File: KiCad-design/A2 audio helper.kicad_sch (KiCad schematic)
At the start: 37 parts, among them J1 PIN HEADER 1x2, J10 PIN HEADER 1x2, J11 PIN HEADER 1x3, J12 PIN HEADER 1x3, J13 PIN HEADER 2x4, J14 PIN HEADER 1x3, J15 PIN HEADER 2x6, J2 PIN HEADER 1x2, J3 PIN HEADER 1x2, J4 SJ1-3515N, J5 PIN HEADER 1x3, J6 PIN HEADER 1x3, J7 SJ1-3515N, J8 PIN HEADER 1x5, J9 PIN HEADER 1x2, K1 SR11-5V-200-2C, SW2 SW_DPDT_x2, U1 pam8403

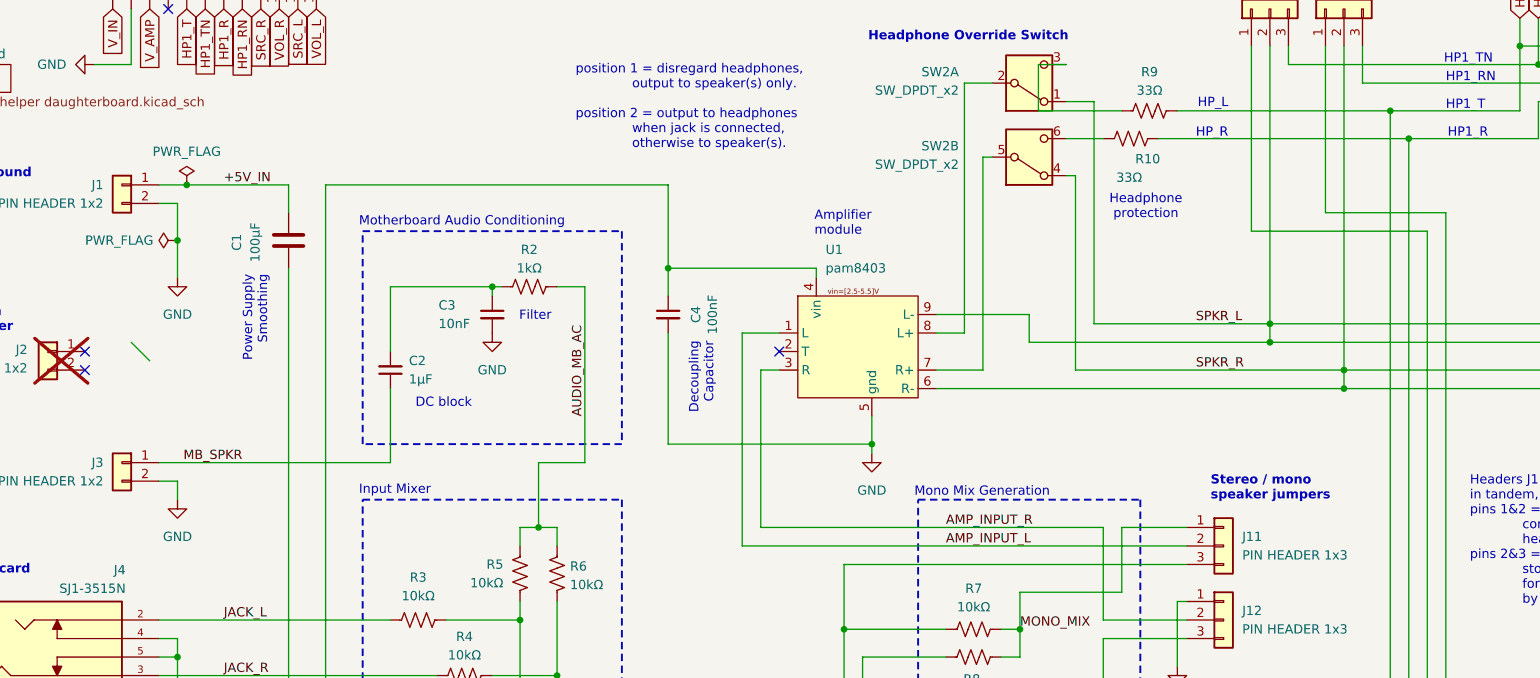
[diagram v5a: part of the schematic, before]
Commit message: fixed mb spkr pin 2 which isnt ground afterall
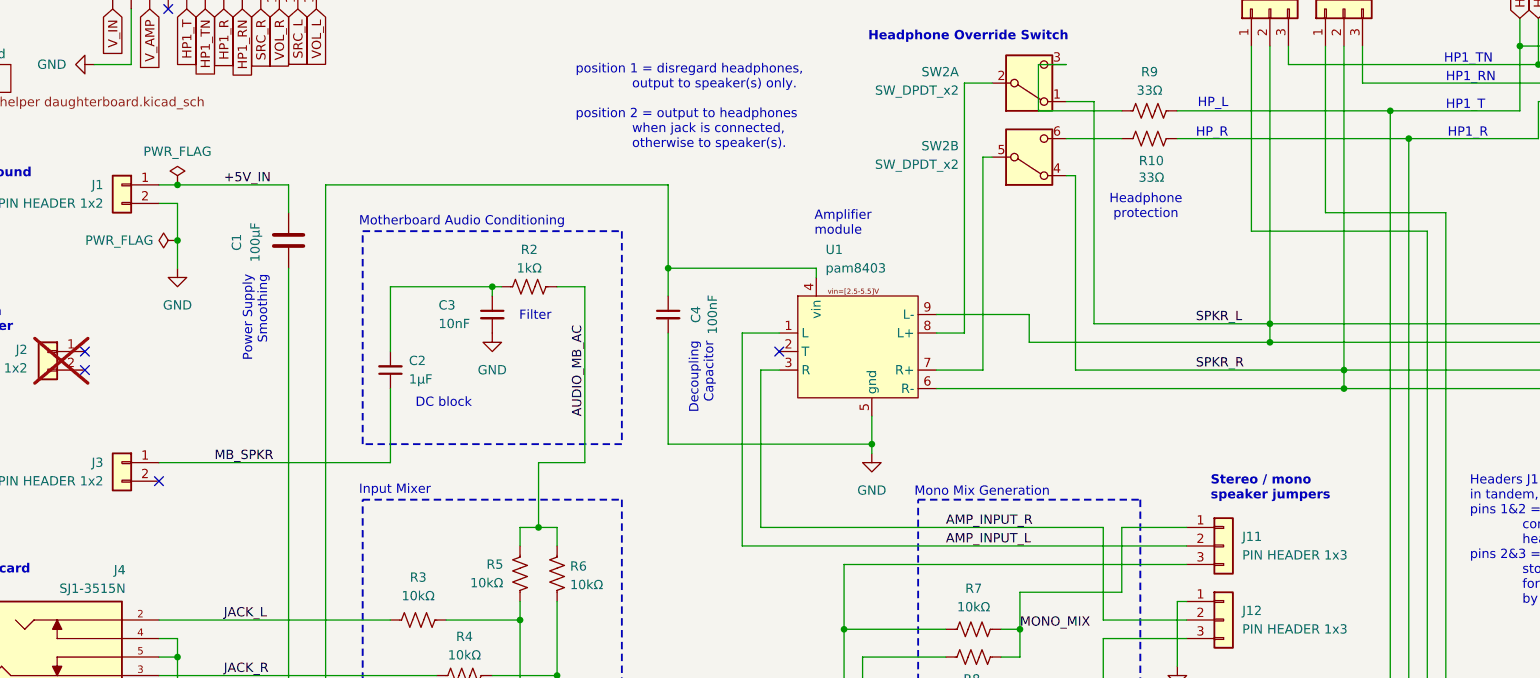
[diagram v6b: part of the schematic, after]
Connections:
- net GND: no longer J3.2 (Pin_2)
- no-connect marks 12 -> 13
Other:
- moved on the sheet: R10
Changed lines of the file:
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@@
 		(title "Apple 2 Audio Helper")
 		(date "2026-02-18")
-		(rev "0.10.4")
+		(rev "0.10.5")
 		(company "Northwest Retroventures")
 		(comment 1 "Optionally supports second internal speaker for stereo.")
@@
 	)
 	(junction
-		(at 54.61 52.07)
-		(diameter 0)
-		(color 0 0 0 0)
-	)
-	(junction
 		(at 105.41 119.38)
 		(diameter 0)
@@
 	)
 	(junction
+		(at 53.34 52.07)
+		(diameter 0)
+		(color 0 0 0 0)
+	)
+	(junction
 		(at 168.91 113.03)
 		(diameter 0)
@@
 	)
 	(no_connect
+		(at 50.8 92.71)
+	)
+	(no_connect
 		(at 257.81 58.42)
 	)
@@
 		(at 257.81 139.7)
 	)
-	(bus_entry
-		(at 46.99 73.66)
-		(size 2.54 2.54)
-		(stroke
-			(width 0)
-			(type default)
-		)
-	)
 	(wire
 		(pts
@@
 	(wire
 		(pts
-			(xy 175.26 45.72) (xy 180.34 45.72)
+			(xy 175.26 45.72) (xy 182.88 45.72)
 		)
 		(stroke
@@
 	(wire
 		(pts
-			(xy 54.61 52.07) (xy 68.58 52.07)
-		)
-		(stroke
-			(width 0)
-			(type default)
-		)
-	)
-	(wire
-		(pts
 			(xy 68.58 151.13) (xy 68.58 153.67)
 		)
@@
 	(wire
 		(pts
-			(xy 53.34 92.71) (xy 53.34 95.25)
-		)
-		(stroke
-			(width 0)
-			(type default)
-		)
-	)
-	(wire
-		(pts
 			(xy 107.95 163.83) (xy 107.95 172.72)
 		)
@@
 	(wire
 		(pts
-			(xy 50.8 52.07) (xy 54.61 52.07)
+			(xy 50.8 52.07) (xy 53.34 52.07)
 		)
 		(stroke
@@
 	(wire
 		(pts
-			(xy 187.96 45.72) (xy 222.25 45.72)
+			(xy 190.5 45.72) (xy 222.25 45.72)
 		)
 		(stroke
@@
 	(wire
 		(pts
-			(xy 53.34 59.69) (xy 53.34 64.77)
+			(xy 53.34 59.69) (xy 53.34 63.5)
 		)
 		(stroke
@@
 	(wire
 		(pts
-			(xy 53.34 92.71) (xy 50.8 92.71)
-		)
-		(stroke
-			(width 0)
-			(type default)
-		)
-	)
-	(wire
-		(pts
 			(xy 50.8 116.84) (xy 53.34 116.84)
 		)
@@
 	(wire
 		(pts
+			(xy 53.34 52.07) (xy 68.58 52.07)
+		)
+		(stroke
+			(width 0)
+			(type default)
+		)
+	)
+	(wire
+		(pts
 			(xy 182.88 107.95) (xy 182.88 99.06)
 		)
@@
 	)
 	(label "MB_SPKR"
-		(at 62.23 90.17 180)
+		(at 58.42 90.17 0)
 		(effects
 			(font
 				(size 1.27 1.27)
 			)
-			(justify right bottom)
+			(justify left bottom)
 		)
 	)
@@
 	(symbol
 		(lib_id "power:GND")
-		(at 53.34 64.77 0)
+		(at 53.34 63.5 0)
 		(unit 1)
 		(exclude_from_sim no)
@@
 		(fields_autoplaced yes)
 		(property "Reference" "#PWR01"
-			(at 53.34 71.12 0)
+			(at 53.34 69.85 0)
 			(effects
 				(font
@@
 		)
 		(property "Value" "GND"
-			(at 53.34 69.85 0)
+			(at 53.34 68.58 0)
 			(effects
 				(font
@@
 		)
 		(property "Footprint" ""
-			(at 53.34 64.77 0)
+			(at 53.34 63.5 0)
 			(effects
 				(font
@@
 		)
 		(property "Datasheet" ""
-			(at 53.34 64.77 0)
+			(at 53.34 63.5 0)
 			(effects
 				(font
@@
 		)
 		(property "Description" "Power symbol creates a global label with name \"GND\" , ground"
-			(at 53.34 64.77 0)
+			(at 53.34 63.5 0)
 			(effects
 				(font
@@
 	(symbol
 		(lib_id "Device:R_US")
-		(at 184.15 45.72 90)
+		(at 186.69 45.72 90)
 		(unit 1)
 		(exclude_from_sim no)
@@
 		(dnp no)
 		(property "Reference" "R10"
-			(at 186.436 48.514 90)
+			(at 186.944 48.768 90)
 			(effects
 				(font
@@
 		)
 		(property "Value" "33Ω"
-			(at 183.896 51.054 90)
+			(at 186.944 51.054 90)
 			(effects
 				(font
@@
 		)
 		(property "Footprint" "Resistor_THT:R_Axial_DIN0207_L6.3mm_D2.5mm_P10.16mm_Horizontal"
-			(at 184.404 44.704 90)
+			(at 186.944 44.704 90)
 			(effects
 				(font
@@
 		)
 		(property "Datasheet" "~"
-			(at 184.15 45.72 0)
+			(at 186.69 45.72 0)
 			(effects
 				(font
@@
 		)
 		(property "Description" "Resistor, US symbol"
-			(at 184.15 45.72 0)
+			(at 186.69 45.72 0)
 			(effects
 				(font
@@
 	(symbol
 		(lib_id "power:PWR_FLAG")
-		(at 54.61 52.07 0)
+		(at 53.34 52.07 0)
 		(unit 1)
 		(exclude_from_sim no)
@@
 		(dnp no)
 		(property "Reference" "#FLG01"
-			(at 54.61 50.165 0)
+			(at 53.34 50.165 0)
 			(effects
 				(font
@@
 		)
 		(property "Value" "PWR_FLAG"
-			(at 54.61 47.498 0)
+			(at 53.34 47.498 0)
 			(effects
 				(font
@@
 		)
 		(property "Footprint" ""
-			(at 54.61 52.07 0)
+			(at 53.34 52.07 0)
 			(effects
 				(font
@@
 		)
 		(property "Datasheet" "~"
-			(at 54.61 52.07 0)
+			(at 53.34 52.07 0)
 			(effects
 				(font
@@
 		)
 		(property "Description" "Special symbol for telling ERC where power comes from"
-			(at 54.61 52.07 0)
+			(at 53.34 52.07 0)
 			(effects
 				(font
@@
 					(unit 1)
 				)
-			)
-		)
-	)
-	(symbol
-		(lib_id "power:GND")
-		(at 53.34 95.25 0)
-		(unit 1)
-		(exclude_from_sim no)
-		(in_bom yes)
-		(on_board yes)
-		(dnp no)
-		(fields_autoplaced yes)
-		(property "Reference" "#PWR02"
-			(at 53.34 101.6 0)
-			(effects
-				(font
-					(size 1.27 1.27)
-				)
-				(hide yes)
-			)
-		)
-		(property "Value" "GND"
-			(at 53.34 100.33 0)
-			(effects
-				(font
-					(size 1.27 1.27)
-				)
-			)
-		)
-		(property "Footprint" ""
-			(at 53.34 95.25 0)
-			(effects
-				(font
-					(size 1.27 1.27)
-				)
-				(hide yes)
-			)
-		)
-		(property "Datasheet" ""
-			(at 53.34 95.25 0)
-			(effects
-				(font
-					(size 1.27 1.27)
-				)
-				(hide yes)
-			)
-		)
-		(property "Description" "Power symbol creates a global label with name \"GND\" , ground"
-			(at 53.34 95.25 0)
-			(effects
-				(font
-					(size 1.27 1.27)
-				)
-				(hide yes)
-			)
-		)
-		(pin "1"
-		)
-		(instances
-			(project ""
-				(path "/5bdcff91-125f-4cf8-8ef8-6f244f2a71f5"
-					(reference "#PWR02")
-					(unit 1)
-				)

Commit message: change 3d model for vol knob
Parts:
- R1: footprint PTR902-1020K-A502:TRIM_PTR902-1020K-A502 -> PTN09S2_H10215K1A:TRIM_PTN09S2-H10215K1A
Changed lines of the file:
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@@
 	(title_block
 		(title "Apple 2 Audio Helper")
-		(date "2026-02-18")
-		(rev "0.10.5")
+		(date "2026-02-26")
+		(rev "0.10.6")
 		(company "Northwest Retroventures")
 		(comment 1 "Optionally supports second internal speaker for stereo.")
@@
 			)
 		)
-		(property "Footprint" "PTR902-1020K-A502:TRIM_PTR902-1020K-A502"
+		(property "Footprint" "PTN09S2_H10215K1A:TRIM_PTN09S2-H10215K1A"
 			(at 60.96 161.29 0)
 			(effects

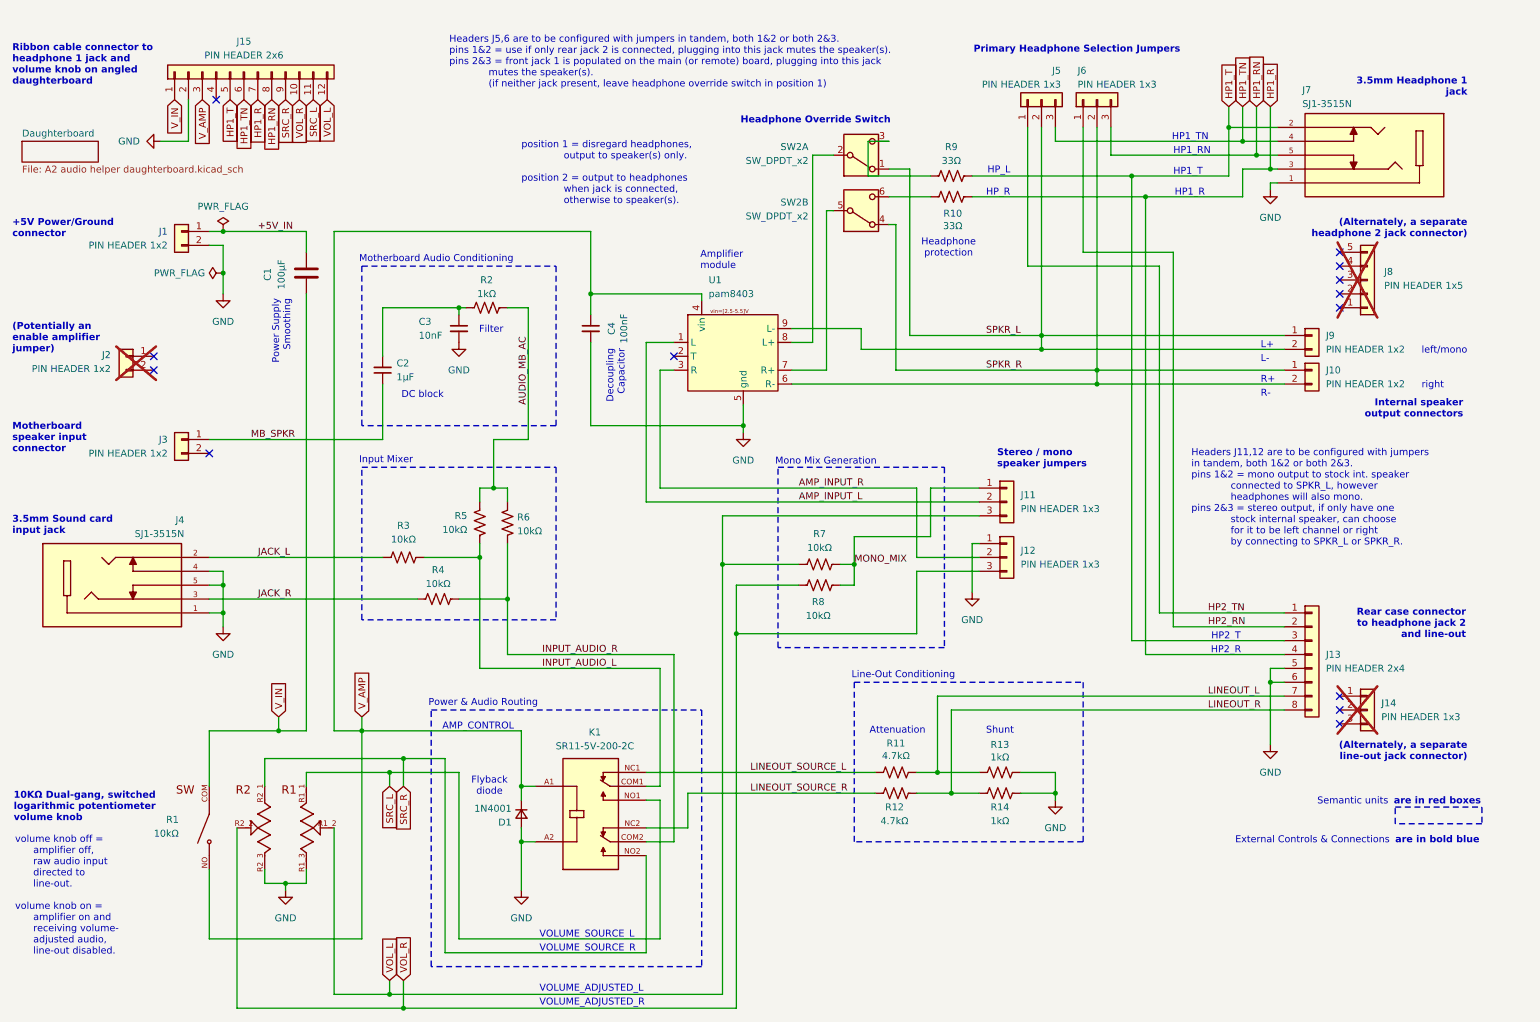
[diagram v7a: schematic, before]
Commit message: picked new part for front hp jack
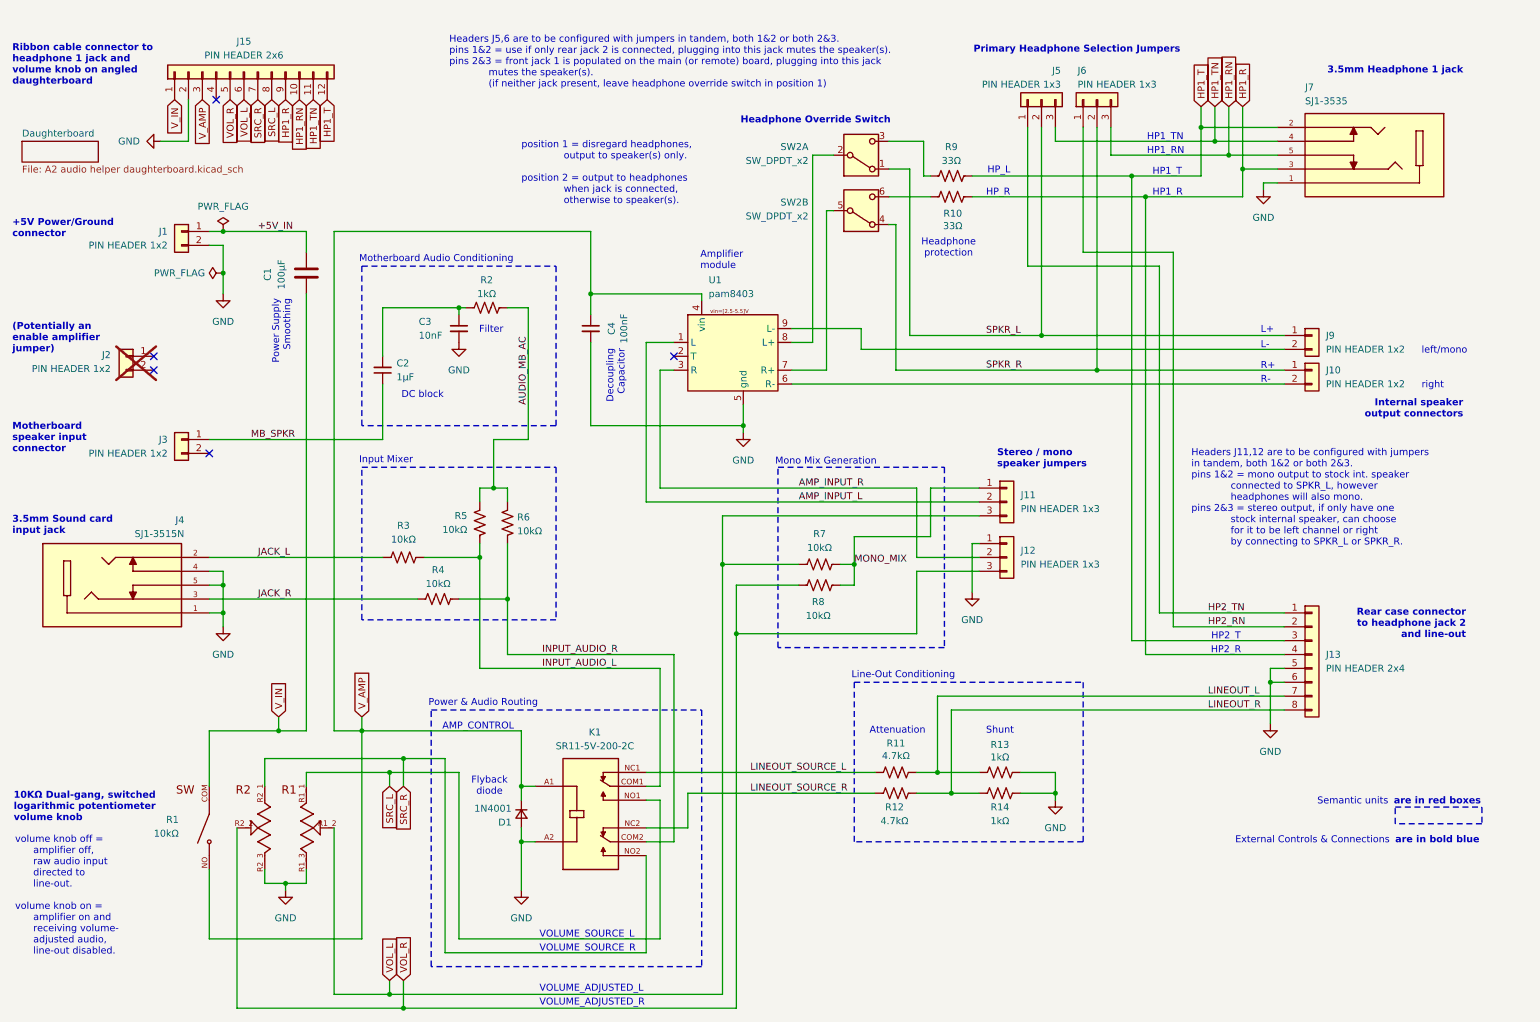
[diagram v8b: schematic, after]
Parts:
- removed J14: PIN HEADER 1x3, Connector_Molex:Molex_KK-254_AE-6410-03A_1x03_P2.54mm_Vertical, symbol Connector_Generic:Conn_01x03
- removed J8: PIN HEADER 1x5, Connector_Molex:Molex_KK-254_AE-6410-05A_1x05_P2.54mm_Vertical, symbol Connector_Generic:Conn_01x05
- J7: value SJ1-3515N -> SJ1-3535; footprint SJ1-3515N:CUI_SJ1-3515N -> SJ1-3535:CUI_SJ1-3535
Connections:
- net HP1_R: now also J15.9 (Pin_9); no longer J15.7 (Pin_7)
- net HP1_RN: now also J15.10 (Pin_10); no longer J15.8 (Pin_8)
- net HP1_T: now also J15.12 (Pin_12); no longer J15.5 (Pin_5)
- net HP1_TN: now also J15.11 (Pin_11); no longer J15.6 (Pin_6)
- net SPKR_L: no longer J9.2 (Pin_2), U1.9 (L-)
- net SPKR_R: no longer J10.2 (Pin_2), U1.6 (R-)
- net SRC_L: now also J15.8 (Pin_8); no longer J15.11 (Pin_11)
- net SRC_R: now also J15.7 (Pin_7); no longer J15.9 (Pin_9)
- net VOL_L: now also J15.6 (Pin_6); no longer J15.12 (Pin_12)
- net VOL_R: now also J15.5 (Pin_5); no longer J15.10 (Pin_10)
- new net: J9.2 (Pin_2), U1.9 (L-)
- new net: J10.2 (Pin_2), U1.6 (R-)
- no-connect marks 13 -> 5
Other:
- note removed: "(Alternately, a separate headphone 2 jack connector)"
- note removed: "(Alternately, a separate line-out jack connector)"
